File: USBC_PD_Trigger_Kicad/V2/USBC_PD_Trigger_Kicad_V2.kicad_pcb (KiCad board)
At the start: 2 copper layers, 42.7 x 46.6 mm, 24 parts, among them J1 USB_C_Receptacle_PowerOnly_6P, J2 Screw_Terminal_01x02, SW1 SW_Push, U1 FUSB302BMPX, U2 ProMicro

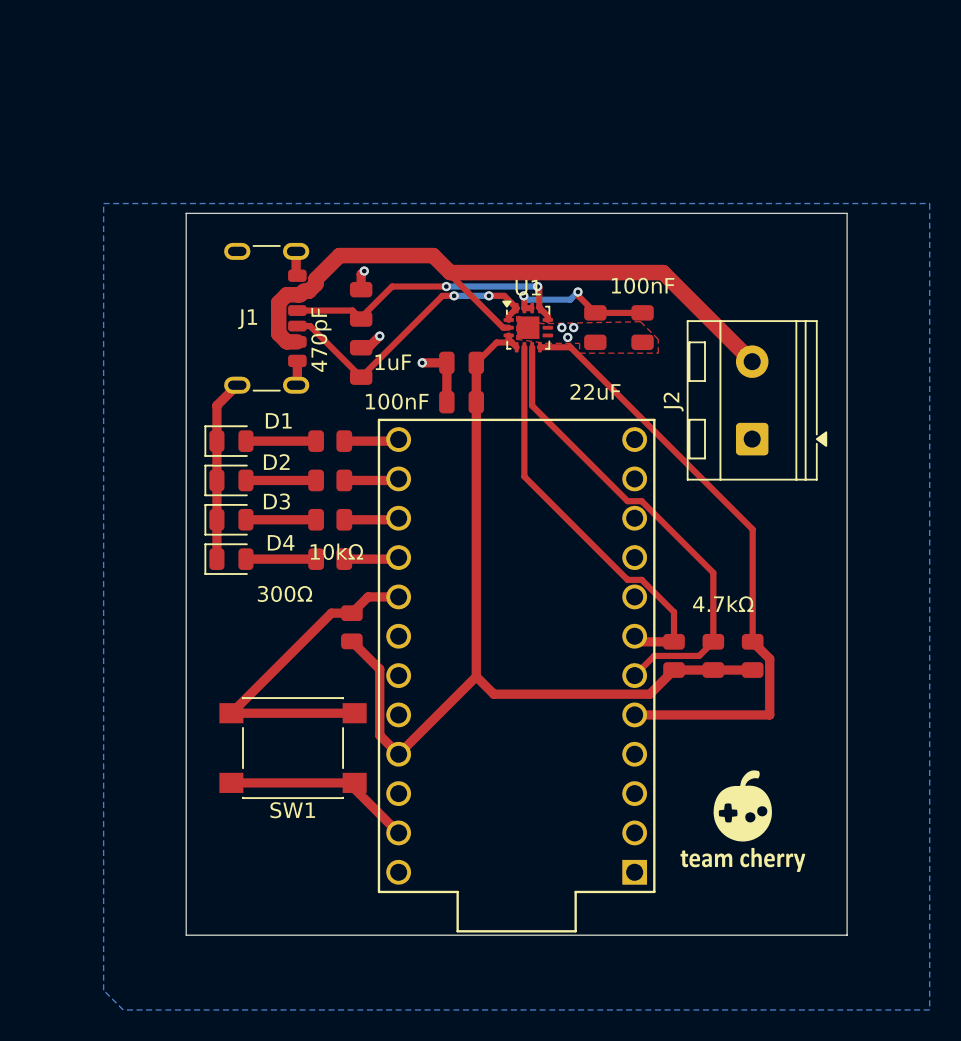
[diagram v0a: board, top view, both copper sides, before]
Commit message: Updated Pd trigger to use only 1 cable
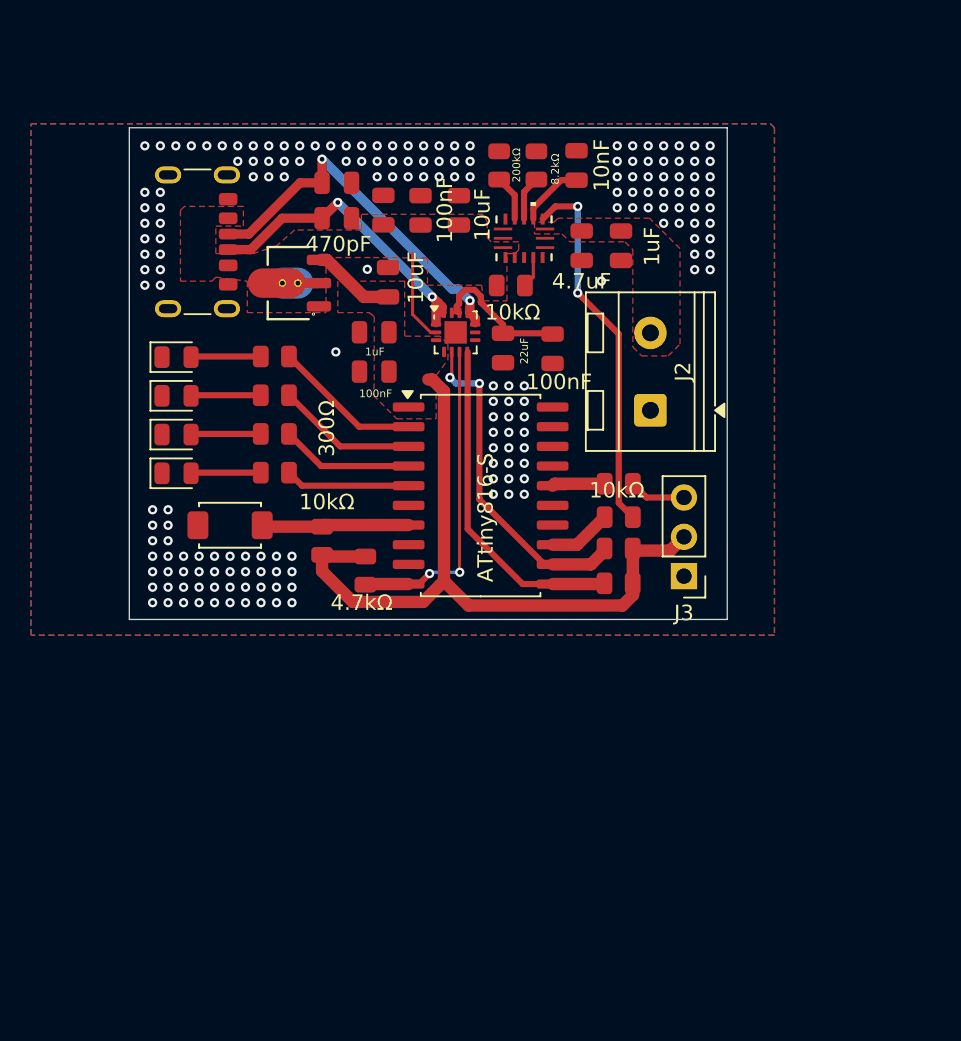
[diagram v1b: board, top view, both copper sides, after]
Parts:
- removed D1, D2, D3, D4: LED, LED_SMD:LED_0805_2012Metric
- removed G***: LOGO, LOGO
- removed R4: 300Ω, PCM_JLCPCB:R_0805
- removed R5: 10kΩ, PCM_JLCPCB:R_0805
- removed Rpu_INT1, Rpu_SCL1, Rpu_SDA1: 4.7kΩ, PCM_JLCPCB:R_0805
- removed SW1: SW_Push, Button_Switch_SMD:SW_SPST_PTS645
- added C10: 1uF, PCM_JLCPCB:C_0805, F.Cu at (126.7, 60.5)
- added C11: 4.7uF, PCM_JLCPCB:C_0805, F.Cu at (124.2, 60.5)
- added C12: 10uF, PCM_JLCPCB:C_0805, F.Cu at (111.4, 58.1)
- added C13: 10uF, PCM_JLCPCB:C_0805, F.Cu at (111.7, 62.8)
- added C2: 10uF, PCM_JLCPCB:C_0805, F.Cu at (116.3, 58.2)
- added C8: 100nF, PCM_JLCPCB:C_0805, F.Cu at (113.8, 58.2)
- added C9: 10nF, PCM_JLCPCB:C_0805, F.Cu at (123.9, 55.3)
- added D5: LED, LED_SMD:LED_0805_2012Metric, F.Cu at (98.0, 67.6)
- added D6: LED, LED_SMD:LED_0805_2012Metric, F.Cu at (98.0, 70.1)
- added D7: LED, LED_SMD:LED_0805_2012Metric, F.Cu at (98.0, 72.6)
- added D8: LED, LED_SMD:LED_0805_2012Metric, F.Cu at (98.0, 75.1)
- added J3: Conn_01x03_Pin, Connector_PinHeader_2.54mm:PinHeader_1x03_P2.54mm_Vertical, F.Cu at (130.8, 81.8)
- added R10: 10kΩ, PCM_JLCPCB:R_0805, F.Cu at (107.4, 79.5)
- added R11: 300Ω, PCM_JLCPCB:R_0805, F.Cu at (104.4, 67.6)
- added R12: 300Ω, PCM_JLCPCB:R_0805, F.Cu at (104.4, 70.1)
- added R13: 300Ω, PCM_JLCPCB:R_0805, F.Cu at (104.4, 72.6)
- added R14: 300Ω, PCM_JLCPCB:R_0805, F.Cu at (104.4, 75.1)
- added R6: 10kΩ, PCM_JLCPCB:R_0805, F.Cu at (119.6, 63.0)
- added R7: 8.2kΩ, PCM_JLCPCB:R_0805, F.Cu at (121.3, 55.3)
- added R8: 10kΩ, PCM_JLCPCB:R_0805, F.Cu at (126.6, 78.0)
- added R9: 200kΩ, PCM_JLCPCB:R_0805, F.Cu at (118.9, 55.3)
- added RPA0: 4.7kΩ, PCM_JLCPCB:R_0805, F.Cu at (126.6, 75.8)
- added S1: Tactile Button, 160gf, PCM_JLCPCB:SW_TS-1088-AR02016, F.Cu at (101.5, 78.5)
- added U3: LS2406ERQ23, footprints:QFN16L_2P5X3P2-0P6_LTF, F.Cu at (120.5, 60.0)
- added U4: ATtiny816-S, Package_SO:SOIC-20W_7.5x12.8mm_P1.27mm, F.Cu at (117.7, 76.6)
- R1, R2, R3: value 300Ω -> 4.7kΩ
- U2: value ProMicro -> HT7533; footprint promicro:ProMicro -> PCM_JLCPCB:SOT-89-3_L4.5-W2.5-P1.50-LS4.2-BR
- moved U2 27.9 mm to (105.9, 62.9), turned to 0 degrees
- moved R1 20.8 mm to (126.6, 82.2)
- moved R3 18.7 mm to (126.6, 80.0)
- moved C6 9.45 mm to (108.4, 58.7), turned to 0 degrees
- moved C7 8.01 mm to (108.4, 56.4), turned to 0 degrees
- moved J2 6.83 mm to (128.6, 71.1)
- moved J1 6.66 mm to (98.3, 60.2)
- moved R2 6.25 mm to (110.2, 81.4), turned to 90 degrees
- moved C3 6.11 mm to (119.1, 67.1)
- moved C5 5.98 mm to (110.8, 68.6)
- moved C4 5.98 mm to (110.8, 66.0)
- moved C1 5.97 mm to (122.3, 67.1)
- moved U1 4.70 mm to (116.1, 66.0)
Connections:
- C4 pad 2: VDD -> VCC
- C5 pad 1: VDD -> VCC
- J2 pad 2: /VBUS -> /VOUT
- R1 pad 1: Net-(D1-A) -> /SDA
- R1 pad 2: /IO1 -> VCC
- R2 pad 1: Net-(D2-A) -> /SCL
- R2 pad 2: /IO2 -> VCC
- R3 pad 1: Net-(D3-A) -> /INT_N
- R3 pad 2: /IO3 -> VCC
- U1 pad 3: VDD -> VCC
- U1 pad 4: VDD -> VCC
- U2 pad 1: unconnected-(U2-TX-Pad1) -> GND
- U2 pad 2: unconnected-(U2-RX-Pad2) -> /VBUS
- U2 pad 3: GND -> VCC
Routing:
- net VDD: track 58.7 -> 0.00 mm
- net VCC: track 0.00 -> 51.7 mm
- net /VBUS: track 43.6 -> 5.92 mm
- net GND: track 34.6 -> 0.00 mm, vias 6 -> 178
- net Net-(U3-FLTB): track 0.00 -> 24.1 mm, vias 0 -> 2
- net /SDA: track 39.8 -> 21.8 mm
- net /IO5: track 21.9 -> 9.54 mm
- net /SCL: track 30.4 -> 20.7 mm, vias 0 -> 2
- net /IO4: track 3.55 -> 9.60 mm
- net /IO3: track 3.55 -> 9.09 mm
- net /IO2: track 3.55 -> 8.58 mm
- net /INT_N: track 26.2 -> 21.4 mm, vias 0 -> 2
- net /CC1: track 19.1 -> 23.9 mm
- net Net-(D4-A): track 4.53 -> 0.00 mm
- net Net-(D3-A): track 4.53 -> 0.00 mm
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- added copper zone on F.Cu, net /VBUS
- added copper zone on F.Cu, net /VOUT
- added copper zone on F.Cu, net VCC
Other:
- board size 42.7 x 46.6 mm -> 38.6 x 31.7 mm

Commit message: Added Code
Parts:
- added REF**: QFN16L_2P5X3P2-0P6_LTF, footprints:QFN16L_2P5X3P2-0P6_LTF-L, F.Cu at (95.0, 49.5)
